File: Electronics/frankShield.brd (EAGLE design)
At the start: 78.4 x 61 mm, 9 parts, among them IC1 BD6230F, IC2 BD6230F

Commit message: 1st hack at the shield design for WiFi Frank...
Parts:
- added C1: 1uF, rcl:C0805
- added IC3: TS5A23157, reprapltd:MSOP10
- added JP6: (no value), pinhead:1X02
- added R1, R3: 15K, rcl:M0805
- added R2: 10K, rcl:M0805
- added S1: TL36PO, switch:TL3XPO
- moved JP2 26.5 mm to (29.2, 21.6), turned to 90 degrees
- moved IC1 26.1 mm to (36.8, 21.6), turned to 0 degrees
- moved JP5 22.2 mm to (12.7, 16.5), turned to 90 degrees
- moved JP3 19.8 mm to (29.2, 44.5), turned to 90 degrees
- moved C3 15.5 mm to (55.9, 17.8)
- moved JP1 11.5 mm to (71.1, 19.1), turned to 270 degrees
- moved IC2 6.35 mm to (36.8, 44.5), turned to 0 degrees
- moved JP4 2.01 mm to (66.7, 50.2)
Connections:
- removed net GND2: U$1.GND2
- new net N$11: IC3.10, U$1.A0
- new net N$12: C1.1, IC3.2, R1.1, R2.2
- new net N$13: JP1.2, S1.2
- new net N$14: IC3.9, JP6.1, R3.1
- new net N$15: IC3.1, U$1.D2
- new net NC2: IC3.7
- net +3V3: now also IC3.8, R3.2
- net GND: now also C1.2, IC3.3, JP6.2, R2.1, U$1.GND2
- net N$7: now also U$1.D6; no longer U$1.D5
- net N$8: now also U$1.D5; no longer U$1.D6
- net V+: now also R1.2, S1.3; no longer JP1.2
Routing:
- net V+: track 0.00 -> 101.5 mm
- net +3V3: track 0.00 -> 67.9 mm, vias 0 -> 1
- net N$11: track 0.00 -> 53.6 mm
- net N$8: track 0.00 -> 53.5 mm
- net N$7: track 0.00 -> 46.5 mm
- net N$15: track 0.00 -> 46.3 mm, vias 0 -> 1
- net N$9: track 0.00 -> 29.3 mm
- net N$10: track 0.00 -> 21.5 mm
- net N$1: track 0.00 -> 12.3 mm
- net N$2: track 0.00 -> 12.3 mm
- net N$4: track 0.00 -> 9.21 mm
- net N$6: track 0.00 -> 9.21 mm
- net N$14: track 0.00 -> 8.57 mm
- net N$12: track 0.00 -> 8.11 mm
- net N$3: track 0.00 -> 6.67 mm
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- added copper zone on layer 1, net GND
- added copper zone on layer 16, net GND
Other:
- board text added: "+"
- board text added: "-"
- board text added: "3V3"
- board text added: "Batt"
- board text added: "C"
- board text added: "E"
- board text added: "Frank The Robot EPS8266/Arduino Shield V1.0 reprapltd.com Licence: GPL"
- board text added: "G"
- board text added: "LIDAR"
- board text added: "Left Motor"
- board text added: "Right Motor"
- board text added: "SCL"
- board text added: "SDA"
- board text added: "photo"

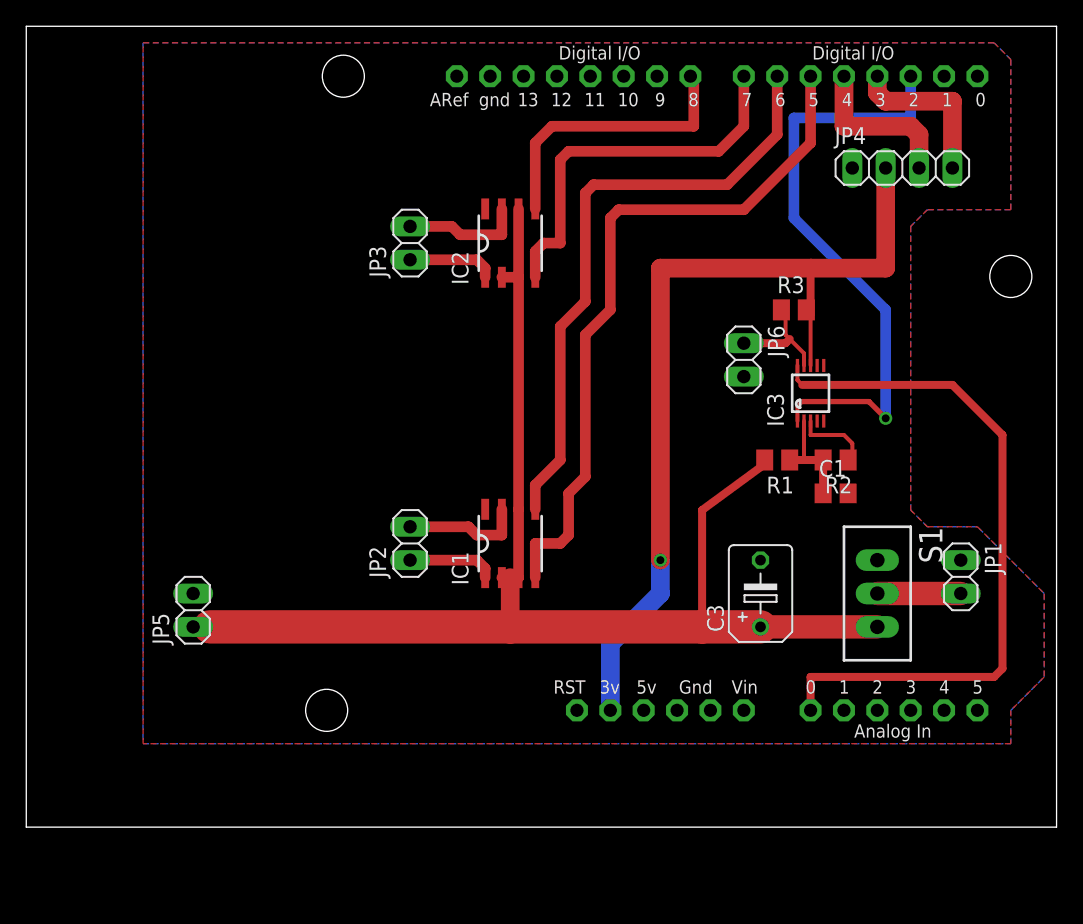
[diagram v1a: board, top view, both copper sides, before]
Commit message: Improved shield design. GERBER files added.
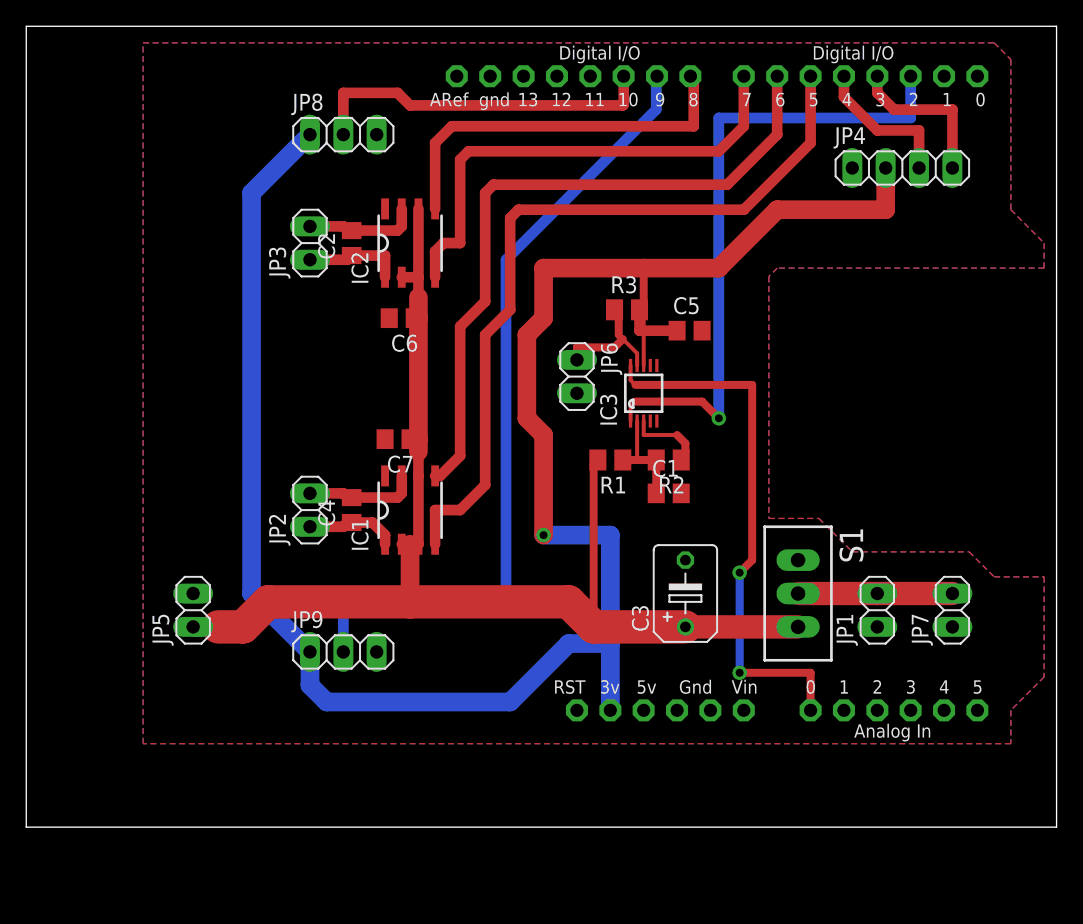
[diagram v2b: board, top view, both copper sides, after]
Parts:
- added C2, C4, C5, C6, C7: 0.1uF, rcl:C0805
- added JP7: (no value), pinhead:1X02
- added JP8, JP9: (no value), pinhead:1X03
- moved JP6 12.8 mm to (41.9, 34.3)
- moved R3 12.7 mm to (45.7, 39.4)
- moved C1 12.7 mm to (48.9, 25.4)
- moved IC3 12.7 mm to (47.0, 33.0)
- moved R1 12.7 mm to (44.5, 27.9)
- moved R2 12.7 mm to (48.9, 27.9)
- moved JP2 8.03 mm to (21.6, 24.1)
- moved IC1 8.03 mm to (29.2, 24.1)
- moved JP3 7.62 mm to (21.6, 44.5)
- moved IC2 7.62 mm to (29.2, 44.5)
- moved JP1 6.84 mm to (64.8, 16.5), turned to 90 degrees
- moved S1 6.03 mm to (58.7, 17.8)
- moved C3 5.72 mm to (50.2, 17.8)
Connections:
- new net N$17: JP9.2, U$1.D9
- new net N$18: JP8.2, U$1.D10
- net +3V3: now also C5.1, JP8.1, JP9.1
- net GND: now also C5.2, C6.2, C7.2, JP7.1, JP8.3, JP9.3
- net N$13: now also JP7.2
- net N$3: now also C2.1, IC2.1, JP3.1; no longer IC1.1, JP2.1
- net N$4: now also C2.2, IC2.7, JP3.2; no longer IC1.7, JP2.2
- net N$5: now also C4.1, IC1.1, JP2.1; no longer IC2.1, JP3.1
- net N$6: now also C4.2, IC1.7, JP2.2; no longer IC2.7, JP3.2
- net V+: now also C6.1, C7.1
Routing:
- net +3V3: track 67.9 -> 154.0 mm
- net N$17: track 0.00 -> 60.4 mm
- net N$18: track 0.00 -> 27.1 mm
- net N$11: track 53.6 -> 41.1 mm, vias 0 -> 2
- net N$10: track 21.5 -> 29.1 mm
- net N$9: track 29.3 -> 36.9 mm
- net V+: track 101.5 -> 94.0 mm
- net N$13: track 6.35 -> 11.7 mm
- net N$7: track 46.5 -> 51.8 mm
- net N$8: track 53.5 -> 58.6 mm
- net N$15: track 46.3 -> 49.1 mm
- net N$2: track 12.3 -> 11.2 mm
- net N$14: track 8.57 -> 9.66 mm
- net N$3: track 6.67 -> 7.50 mm
- net N$4: track 9.21 -> 8.58 mm
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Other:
- board text added: "+3V3"
- board text added: "EPS8266/Arduino Shield V1.0 reprapltd.com Mechanics & software: Sally Bowyer Electronics: Adrian Bowyer Licence - GPL"
- board text added: "Frank The Robot"
- board text added: "L. sense"
- board text added: "Pwr"
- board text added: "R. sense"
- board text added: "charge"
- board text added: "sig"
- board text removed: "3V3"
- board text removed: "Frank The Robot EPS8266/Arduino Shield V1.0 reprapltd.com Licence: GPL"
